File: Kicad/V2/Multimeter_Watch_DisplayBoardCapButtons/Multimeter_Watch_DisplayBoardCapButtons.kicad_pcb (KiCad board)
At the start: 2 copper layers, 46 x 42 mm, 22 parts, among them J1 51281-1294, U1 AT42QT1070-S

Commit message: Keepout and silkscreen changes to capacitance top board
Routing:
- net /GND: track 23.4 -> 35.9 mm, vias 2 -> 9
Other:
- board text removed: "PB5"

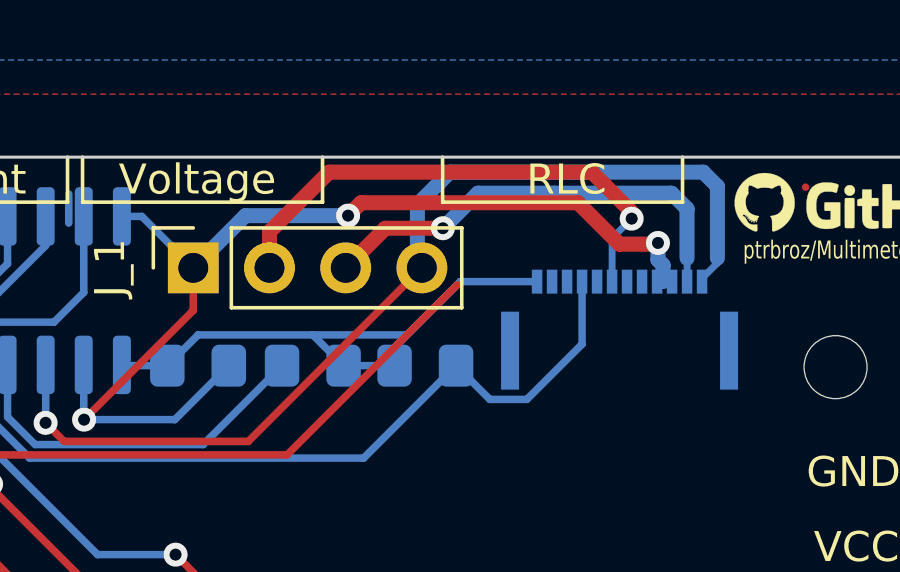
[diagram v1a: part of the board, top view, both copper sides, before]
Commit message: fix flex conn
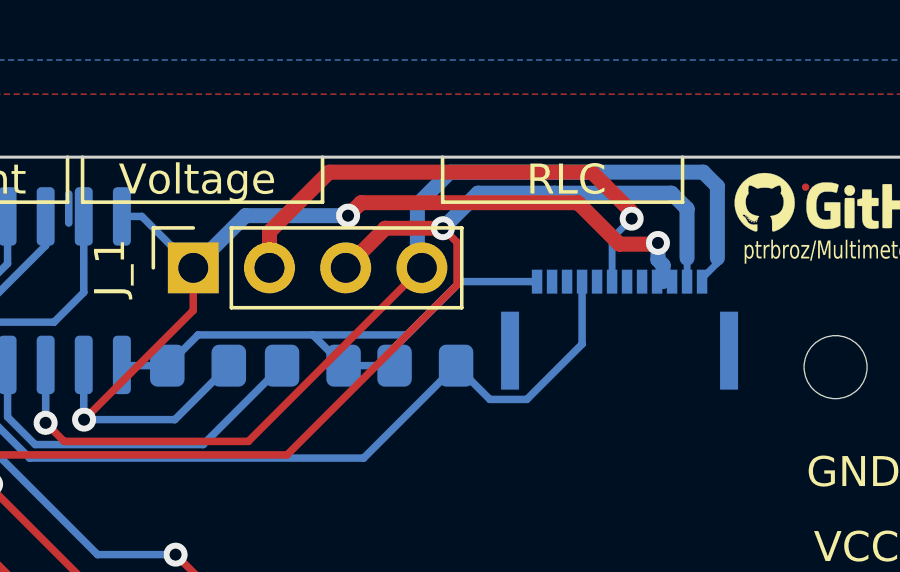
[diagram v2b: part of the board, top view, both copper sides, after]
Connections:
- J1 pad 1: /VCC -> /SDA
- J1 pad 10: /GND -> /PE5
- J1 pad 11: /SCL -> /PE4
- J1 pad 12: /SDA -> /VCC
- J1 pad 2: /PE4 -> /SCL
- J1 pad 3: /PE5 -> /GND
- J1 pad 4: /PB6 -> /GND
- J1 pad 5: /PB7 -> /PD6
- J1 pad 6: /PB5 -> /PD5
- J1 pad 7: /PD5 -> /PB5
- J1 pad 8: /PD6 -> /PB7
- J1 pad 9: /GND -> /PB6
- PAD1 pad 1: Net-(PAD1-Pad1) -> (no net)
- PAD2 pad 1: Net-(PAD2-Pad1) -> (no net)
- R3 pad 1: Net-(PAD2-Pad1) -> Net-(PAD2-Pad~)
- R5 pad 1: Net-(PAD1-Pad1) -> Net-(PAD1-Pad~)
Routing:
- net /SCL: track 37.2 -> 39.3 mm

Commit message: drc update and fixes to capbuttons board
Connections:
- PAD1 pad 1: (no net) -> Net-(PAD1-Pad1)
- PAD2 pad 1: (no net) -> Net-(PAD2-Pad1)
- R3 pad 1: Net-(PAD2-Pad~) -> Net-(PAD2-Pad1)
- R5 pad 1: Net-(PAD1-Pad~) -> Net-(PAD1-Pad1)
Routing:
- net /GND: track 35.9 -> 37.1 mm
- net Net-(R3-Pad2): track 11.9 -> 10.9 mm
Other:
- net class Default: clearance 0.2 -> 0.15
- rule trace_clearance: 0.2 -> 0.15
- rule trace_min: 0.2 -> 0.15

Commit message: make touchpad reference blank
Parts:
- removed PAD1: Touch_Pad, Multimeter_Watch_Custom_Footprints:CapButton_Left
- added  : Touch_Pad, Multimeter_Watch_Custom_Footprints:CapButton_Left, F.Cu at (112.2, 94.0)
-  : renamed from PAD2
